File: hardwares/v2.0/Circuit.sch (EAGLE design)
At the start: 34 parts, among them IC1 TINY24/44/84-PU, IC2 HT-7733A, J1 1X2-3.5MM, Q1 8MHz, T1 2N2222, T2 2N2222, T3 2N2222, T4 2N2222, T5 2N2222, T6 2N2222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

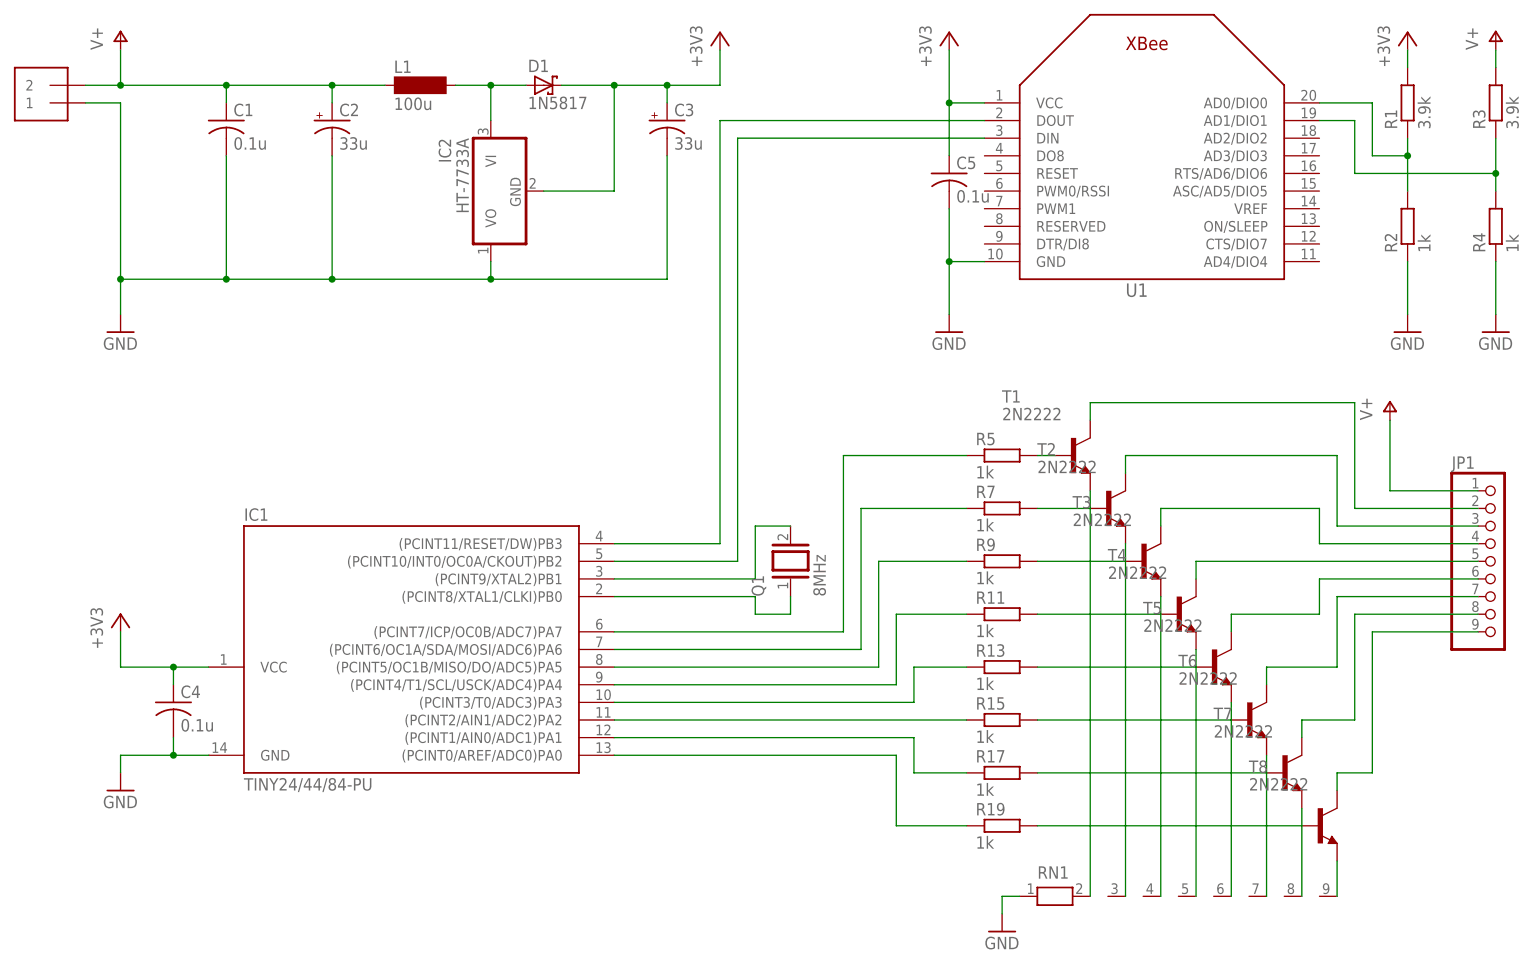
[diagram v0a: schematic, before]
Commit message: Circuit: Add RESET sw
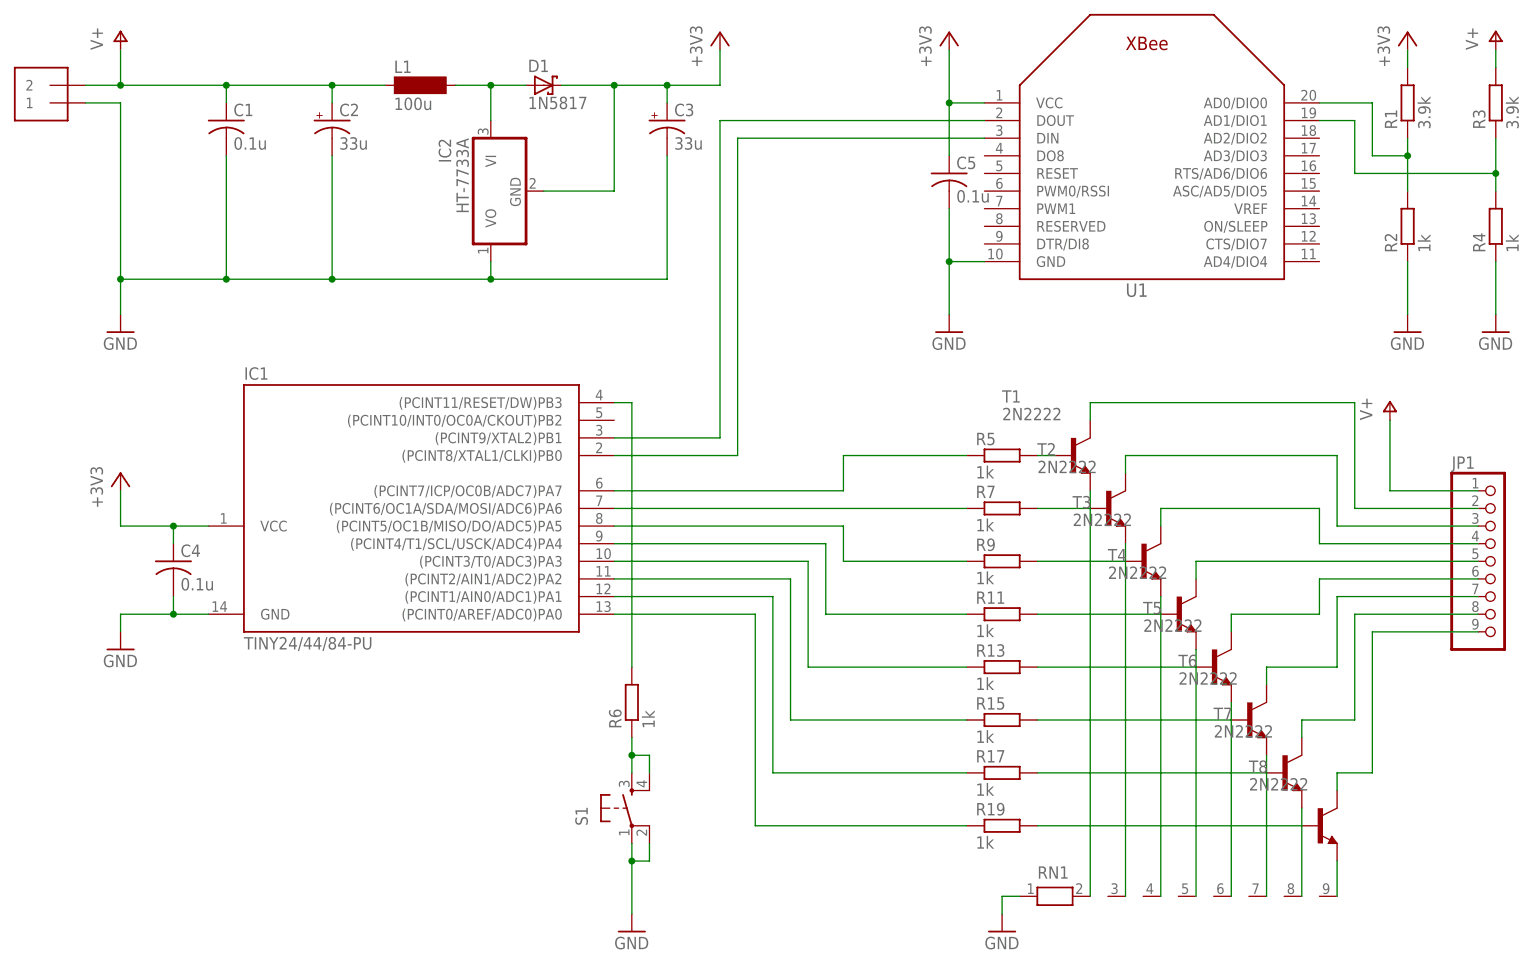
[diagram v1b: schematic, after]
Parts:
- removed Q1: 8MHz, special:XTAL/S
- added R6: 1k, rcl:R-EU_0204/7
- added S1: (no value), SparkFun:TAC_SWITCHPTH
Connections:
- net GND: now also S1.1, S1.2
- net N$1: now also IC1.(PCINT9/XTAL2)PB1; no longer IC1.(PCINT11/RESET/DW)PB3
- net N$2: now also IC1.(PCINT8/XTAL1/CLKI)PB0; no longer IC1.(PCINT10/INT0/OC0A/CKOUT)PB2
- net N$4: now also R6.1, S1.3, S1.4; no longer IC1.(PCINT9/XTAL2)PB1, Q1.2
- net N$5: now also IC1.(PCINT11/RESET/DW)PB3, R6.2; no longer IC1.(PCINT8/XTAL1/CLKI)PB0, Q1.1
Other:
- moved on the sheet: C4, IC1

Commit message: Circuit: NPN Transistors changed
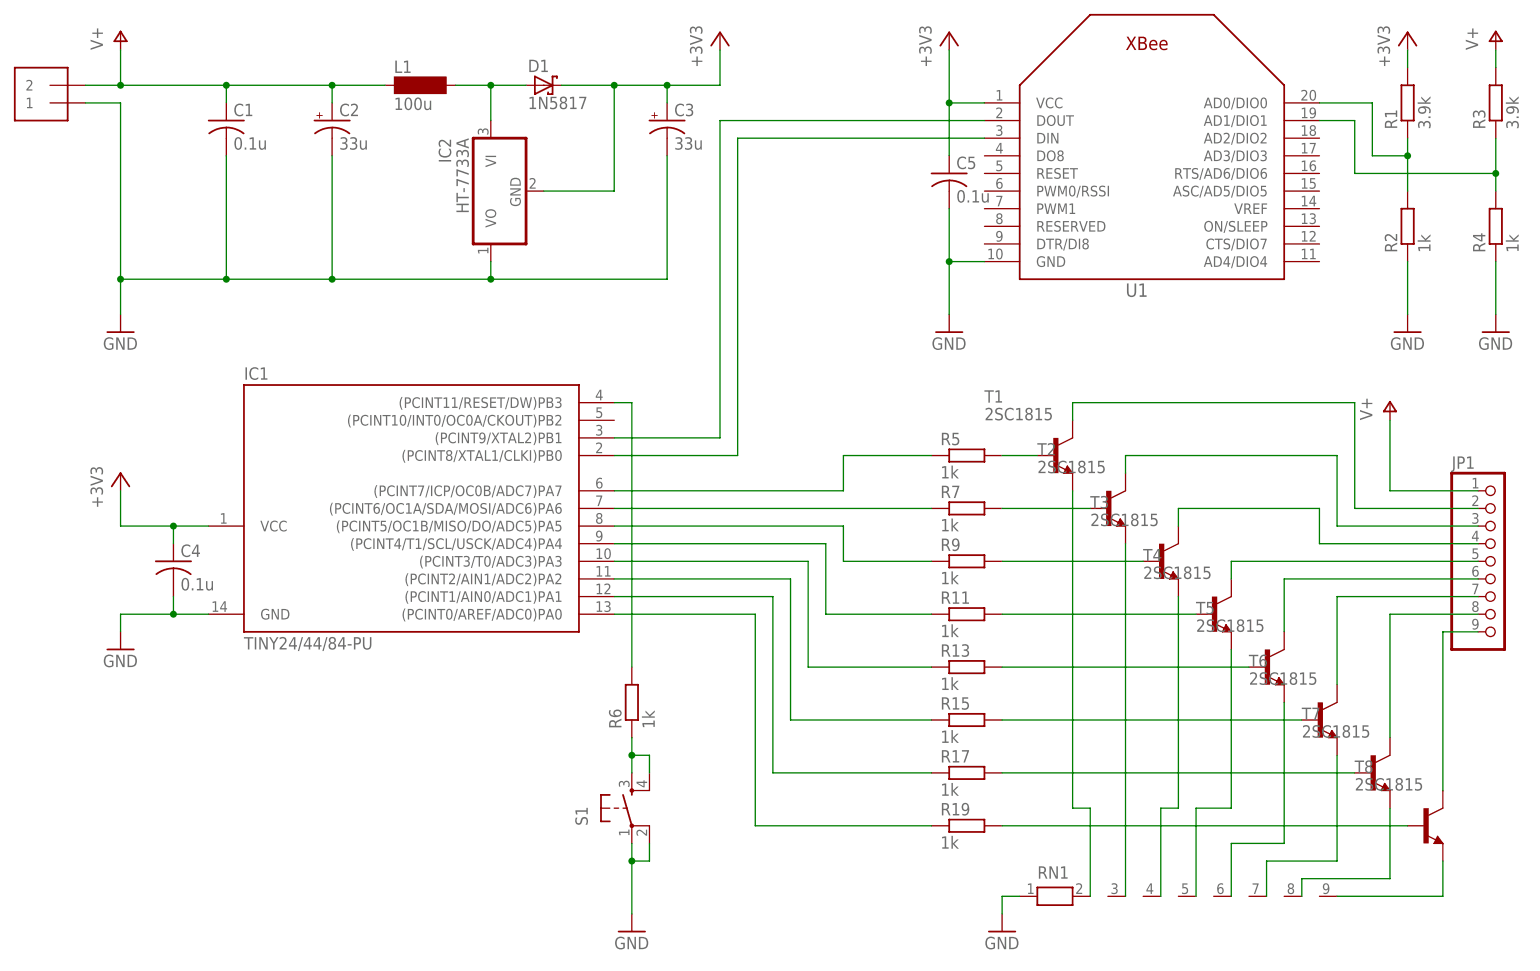
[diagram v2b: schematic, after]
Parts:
- T1, T2, T3, T4, T5, T6, T7, T8: value 2N2222 -> 2SC1815; device adafruit:2N2222 -> transistor:2SC1815
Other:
- moved on the sheet: R11, R13, R15, R17, R19, R5, R7, R9, T1, T3, T4, T5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

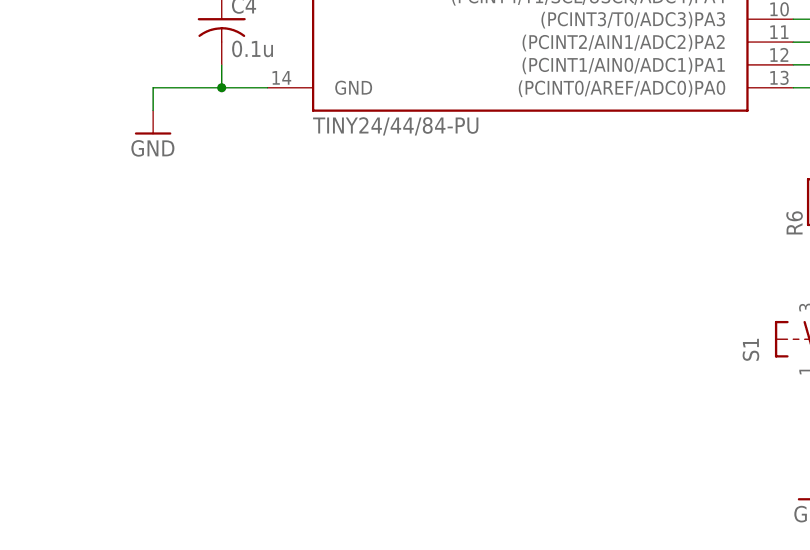
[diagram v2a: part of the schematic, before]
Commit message: Circuit: Rewrite connector added
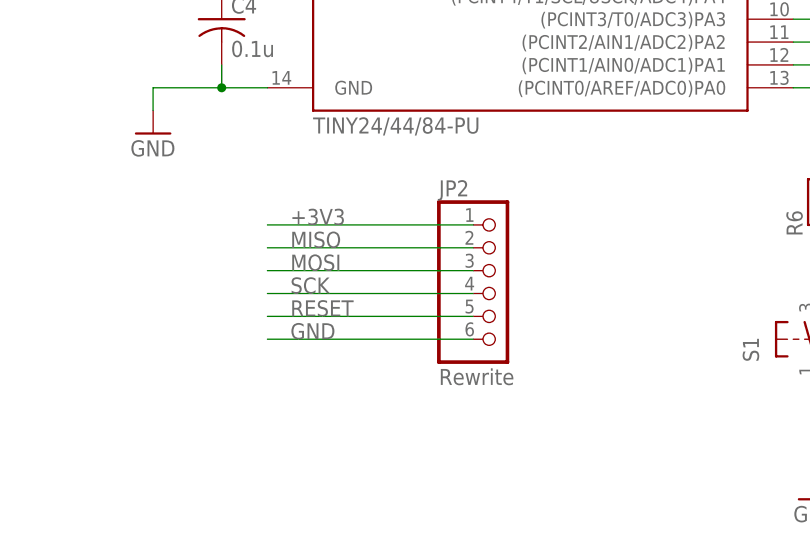
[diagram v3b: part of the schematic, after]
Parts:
- added JP2: Rewrite, adafruit:PINHD-1X6
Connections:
- removed net N$10: IC1.(PCINT6/OC1A/SDA/MOSI/ADC6)PA6, R7.1
- removed net N$19: IC1.(PCINT5/OC1B/MISO/DO/ADC5)PA5, R9.1
- removed net N$22: IC1.(PCINT4/T1/SCL/USCK/ADC4)PA4, R11.1
- removed net N$5: IC1.(PCINT11/RESET/DW)PB3, R6.2
- new net MISO: IC1.(PCINT5/OC1B/MISO/DO/ADC5)PA5, JP2.2, R9.1
- new net MOSI: IC1.(PCINT6/OC1A/SDA/MOSI/ADC6)PA6, JP2.3, R7.1
- new net RESET: IC1.(PCINT11/RESET/DW)PB3, JP2.5, R6.2
- new net SCK: IC1.(PCINT4/T1/SCL/USCK/ADC4)PA4, JP2.4, R11.1
- net +3V3: now also JP2.1
- net GND: now also JP2.6
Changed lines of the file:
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@@
 <part name="T7" library="transistor" deviceset="2SC1815" device=""/>
 <part name="T8" library="transistor" deviceset="2SC1815" device=""/>
+<part name="JP2" library="adafruit" deviceset="PINHD-1X6" device="" value="Rewrite"/>
 </parts>
 <sheets>
@@
 <instance part="T7" gate="G$1" x="203.2" y="20.32"/>
 <instance part="T8" gate="G$1" x="210.82" y="12.7"/>
+<instance part="JP2" gate="A" x="60.96" y="20.32"/>
 </instances>
 <busses>
@@
 <junction x="96.52" y="7.62"/>
 </segment>
+<segment>
+<pinref part="JP2" gate="A" pin="6"/>
+<wire x1="58.42" y1="15.24" x2="35.56" y2="15.24" width="0.1524" layer="91"/>
+<label x="38.1" y="15.24" size="1.778" layer="95"/>
+</segment>
 </net>
 <net name="+3V3" class="0">
@@
 <pinref part="R1" gate="G$1" pin="2"/>
 <wire x1="208.28" y1="124.46" x2="208.28" y2="121.92" width="0.1524" layer="91"/>
+</segment>
+<segment>
+<pinref part="JP2" gate="A" pin="1"/>
+<wire x1="58.42" y1="27.94" x2="35.56" y2="27.94" width="0.1524" layer="91"/>
+<label x="38.1" y="27.94" size="1.778" layer="95"/>
 </segment>
 </net>
@@
 </segment>
 </net>
-<net name="N$19" class="0">
-<segment>
-<pinref part="IC1" gate="1" pin="(PCINT5/OC1B/MISO/DO/ADC5)PA5"/>
-<wire x1="93.98" y1="55.88" x2="127" y2="55.88" width="0.1524" layer="91"/>
-<wire x1="127" y1="55.88" x2="127" y2="50.8" width="0.1524" layer="91"/>
-<pinref part="R9" gate="G$1" pin="1"/>
-<wire x1="127" y1="50.8" x2="139.7" y2="50.8" width="0.1524" layer="91"/>
-</segment>
-</net>
 <net name="N$20" class="0">
 <segment>
@@
 <wire x1="190.5" y1="48.26" x2="218.44" y2="48.26" width="0.1524" layer="91"/>
 <pinref part="T5" gate="G$1" pin="C"/>
-</segment>
-</net>
-<net name="N$22" class="0">
-<segment>
-<wire x1="124.46" y1="53.34" x2="93.98" y2="53.34" width="0.1524" layer="91"/>
-<pinref part="IC1" gate="1" pin="(PCINT4/T1/SCL/USCK/ADC4)PA4"/>
-<wire x1="124.46" y1="53.34" x2="124.46" y2="43.18" width="0.1524" layer="91"/>
-<pinref part="R11" gate="G$1" pin="1"/>
-<wire x1="124.46" y1="43.18" x2="139.7" y2="43.18" width="0.1524" layer="91"/>
 </segment>
 </net>
@@
 <pinref part="R19" gate="G$1" pin="1"/>
 <wire x1="114.3" y1="12.7" x2="139.7" y2="12.7" width="0.1524" layer="91"/>
-</segment>
-</net>
-<net name="N$10" class="0">
-<segment>
-<pinref part="R7" gate="G$1" pin="1"/>
-<pinref part="IC1" gate="1" pin="(PCINT6/OC1A/SDA/MOSI/ADC6)PA6"/>
-<wire x1="139.7" y1="58.42" x2="93.98" y2="58.42" width="0.1524" layer="91"/>
 </segment>
 </net>
@@
 </segment>
 </net>
-<net name="N$5" class="0">
-<segment>
-<pinref part="IC1" gate="1" pin="(PCINT11/RESET/DW)PB3"/>
-<wire x1="93.98" y1="73.66" x2="96.52" y2="73.66" width="0.1524" layer="91"/>
-<pinref part="R6" gate="G$1" pin="2"/>
-<wire x1="96.52" y1="73.66" x2="96.52" y2="35.56" width="0.1524" layer="91"/>
-</segment>
-</net>
 <net name="N$37" class="0">
 <segment>
@@
 </segment>
 </net>
+<net name="MOSI" class="0">
+<segment>
+<pinref part="JP2" gate="A" pin="3"/>
+<wire x1="58.42" y1="22.86" x2="35.56" y2="22.86" width="0.1524" layer="91"/>
+<label x="38.1" y="22.86" size="1.778" layer="95"/>
+</segment>
+<segment>
+<pinref part="R7" gate="G$1" pin="1"/>
+<pinref part="IC1" gate="1" pin="(PCINT6/OC1A/SDA/MOSI/ADC6)PA6"/>
+<wire x1="139.7" y1="58.42" x2="93.98" y2="58.42" width="0.1524" layer="91"/>
+</segment>
+</net>
+<net name="RESET" class="0">
+<segment>
+<pinref part="IC1" gate="1" pin="(PCINT11/RESET/DW)PB3"/>
+<wire x1="93.98" y1="73.66" x2="96.52" y2="73.66" width="0.1524" layer="91"/>
+<pinref part="R6" gate="G$1" pin="2"/>
+<wire x1="96.52" y1="73.66" x2="96.52" y2="35.56" width="0.1524" layer="91"/>
+</segment>
+<segment>
+<pinref part="JP2" gate="A" pin="5"/>
+<wire x1="58.42" y1="17.78" x2="35.56" y2="17.78" width="0.1524" layer="91"/>
+<label x="38.1" y="17.78" size="1.778" layer="95"/>
+</segment>
+</net>
+<net name="MISO" class="0">
+<segment>
+<pinref part="IC1" gate="1" pin="(PCINT5/OC1B/MISO/DO/ADC5)PA5"/>
+<wire x1="93.98" y1="55.88" x2="127" y2="55.88" width="0.1524" layer="91"/>
+<wire x1="127" y1="55.88" x2="127" y2="50.8" width="0.1524" layer="91"/>
+<pinref part="R9" gate="G$1" pin="1"/>
+<wire x1="127" y1="50.8" x2="139.7" y2="50.8" width="0.1524" layer="91"/>
+</segment>
+<segment>
+<pinref part="JP2" gate="A" pin="2"/>
+<wire x1="58.42" y1="25.4" x2="35.56" y2="25.4" width="0.1524" layer="91"/>
+<label x="38.1" y="25.4" size="1.778" layer="95"/>
+</segment>
+</net>
+<net name="SCK" class="0">
+<segment>
+<wire x1="124.46" y1="53.34" x2="93.98" y2="53.34" width="0.1524" layer="91"/>
+<pinref part="IC1" gate="1" pin="(PCINT4/T1/SCL/USCK/ADC4)PA4"/>
+<wire x1="124.46" y1="53.34" x2="124.46" y2="43.18" width="0.1524" layer="91"/>
+<pinref part="R11" gate="G$1" pin="1"/>
+<wire x1="124.46" y1="43.18" x2="139.7" y2="43.18" width="0.1524" layer="91"/>
+</segment>
+<segment>
+<pinref part="JP2" gate="A" pin="4"/>
+<wire x1="58.42" y1="20.32" x2="35.56" y2="20.32" width="0.1524" layer="91"/>
+<label x="38.1" y="20.32" size="1.778" layer="95"/>
+</segment>
+</net>
